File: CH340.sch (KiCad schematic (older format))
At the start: 16 parts, among them J1 USB_OTG, J2 Conn_01x05, U1 CH340T, Y1 CRYSTAL-12MHZ\"

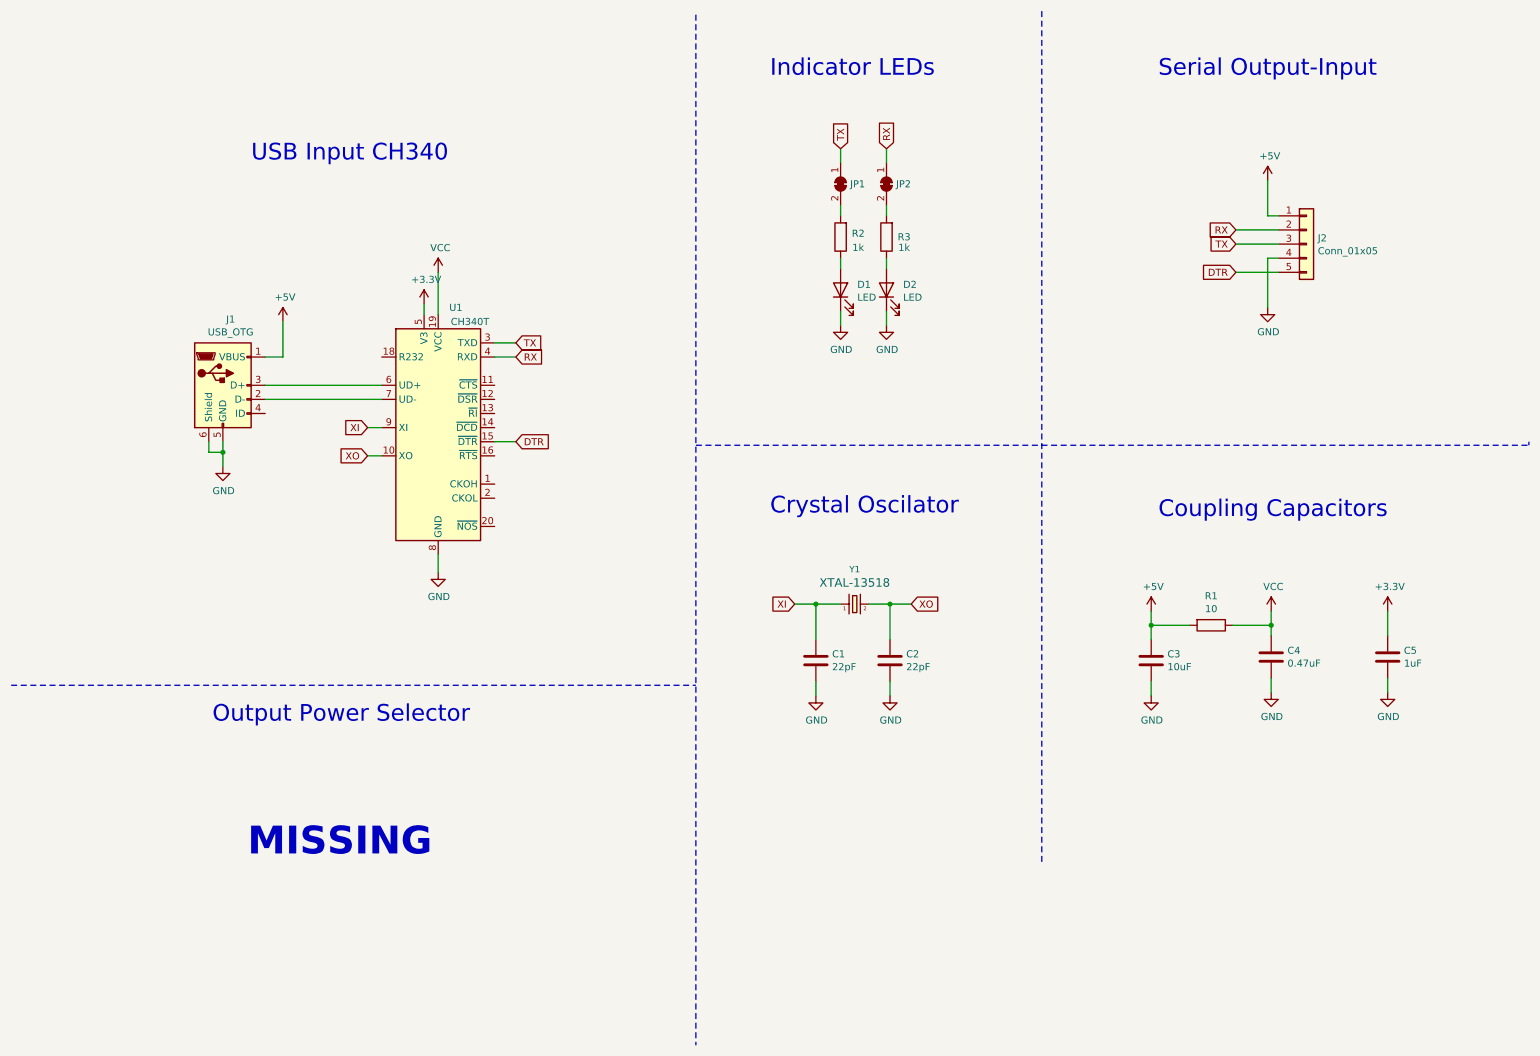
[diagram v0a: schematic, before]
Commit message: Refactory with 3.3v LDO
Signed-off-by: Ricardo Mena C <rgacort12@gmail.com>
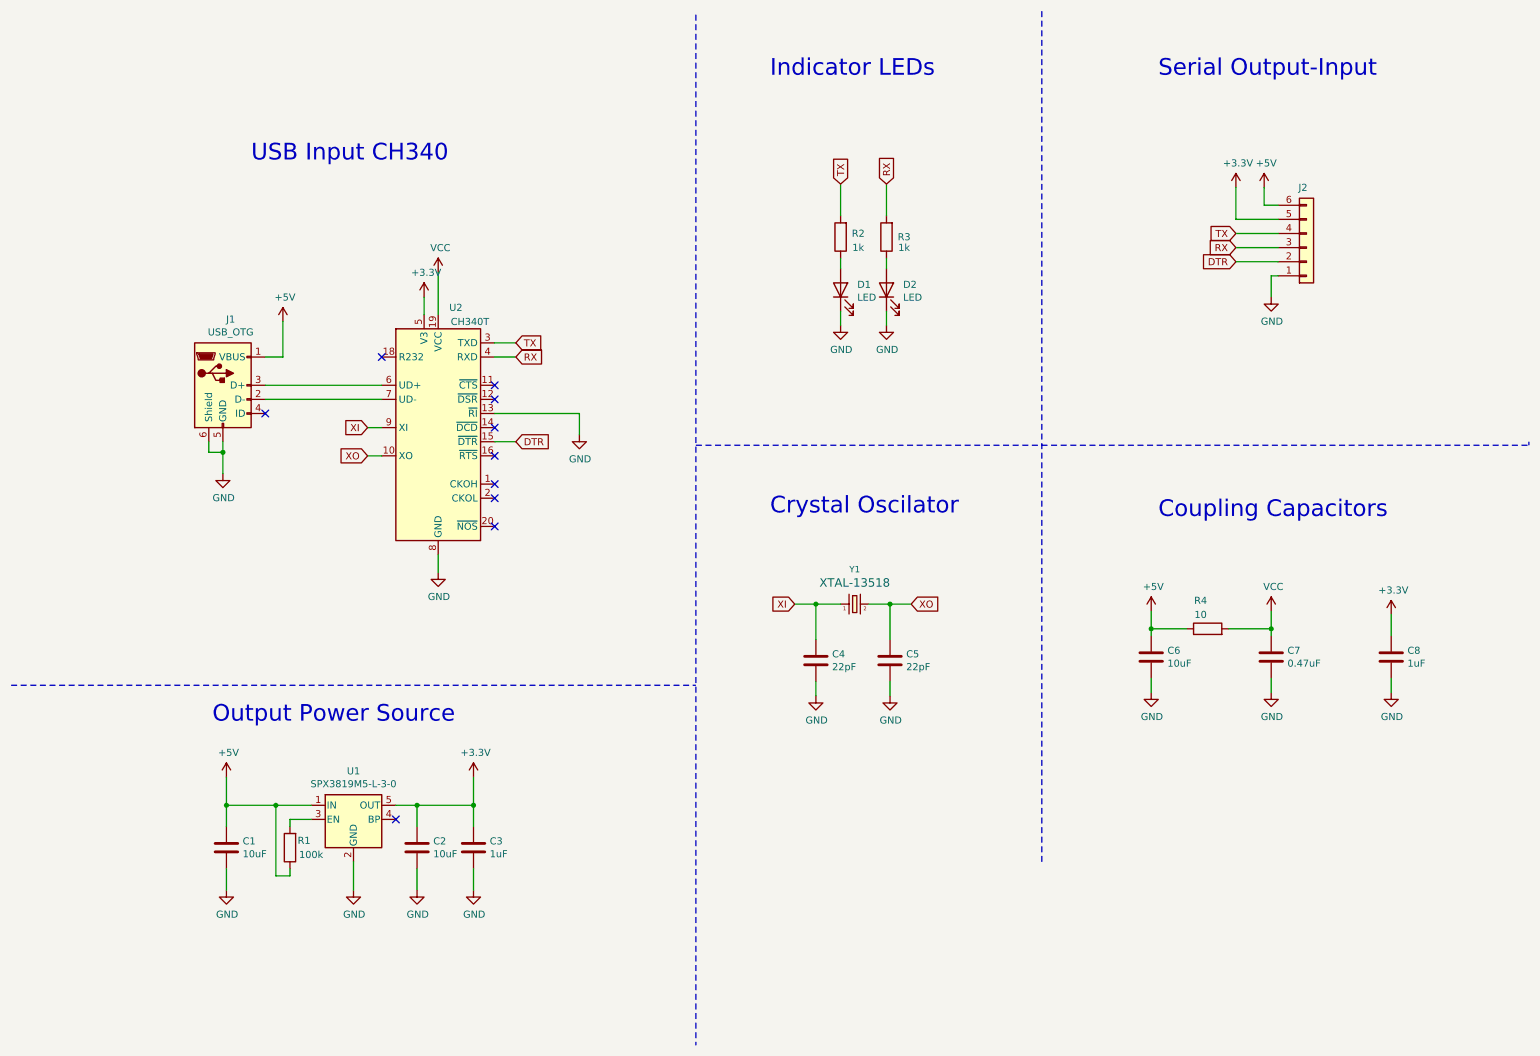
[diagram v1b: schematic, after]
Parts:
- removed J2: Conn_01x05, Connector_PinHeader_2.54mm:PinHeader_1x05_P2.54mm_Horizontal, symbol Connector_Generic:Conn_01x05
- removed JP1, JP2: SolderJumper_2_Bridged, Jumper:SolderJumper-2_P1.3mm_Bridged_RoundedPad1.0x1.5mm, symbol Jumper:SolderJumper_2_Bridged
- added C1, C2: 10uF, Capacitor_SMD:C_0805_2012Metric_Pad1.15x1.40mm_HandSolder, symbol Device:C
- added C3: 1uF, Capacitor_SMD:C_0805_2012Metric_Pad1.15x1.40mm_HandSolder, symbol Device:C
- added J2: Conn_01x06, Connector_PinHeader_2.54mm:PinHeader_1x06_P2.54mm_Horizontal, symbol Connector_Generic:Conn_01x06
- added R4: 10, Resistor_SMD:R_0805_2012Metric_Pad1.15x1.40mm_HandSolder, symbol Device:R
- added U1: SPX3819M5-L-3-0, Package_TO_SOT_SMD:SOT-23-5, symbol Regulator_Linear:SPX3819M5-L-3-0
- J1: lcs (none) -> C132560
- R1: value 10 -> 100k
- U2: renamed from U1; lcs (none) -> C8689
- Y1: Field4 XTAL-13518 -> (none); Fts (none) -> XTAL-13518; lcs (none) -> C254363
- renumbered C1 to C4, C2 to C5, C3 to C6, C4 to C7, C5 to C8
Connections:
- net +3V3: now also C2.2, C3.2, J2.5 (Pin_5), U1.5 (OUT)
- net +5V: now also R1.1, C1.2, J2.6 (Pin_6), R4.1, U1.1 (IN); no longer R1.2
- net DTR: now also J2.2 (Pin_2)
- net GND: now also U2.13 (~RI), C1.1, C2.1, C3.1, J2.1 (Pin_1), U1.2 (GND)
- net RX: now also R3.2, J2.3 (Pin_3)
- net TX: now also R2.2, J2.4 (Pin_4)
- net VCC: now also R4.2; no longer R1.1
- new net: R1.2, U1.3 (EN)
- no-connect marks 0 -> 10
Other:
- note added: "Output Power Source"
- note removed: "MISSING"
- note removed: "Output Power Selector"
- moved on the sheet: C6, C8
